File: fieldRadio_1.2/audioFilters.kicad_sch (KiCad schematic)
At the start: 42 parts, among them U2 OPA1678, U3 OPA1678, U4 OPA1678, U5 OPA1678

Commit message: Starting to update fieldRadio 1.2 schematics
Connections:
- net HPLP Filters/in: no longer U5.6 (-), U5.7
- new net: U5.6 (-), U5.7

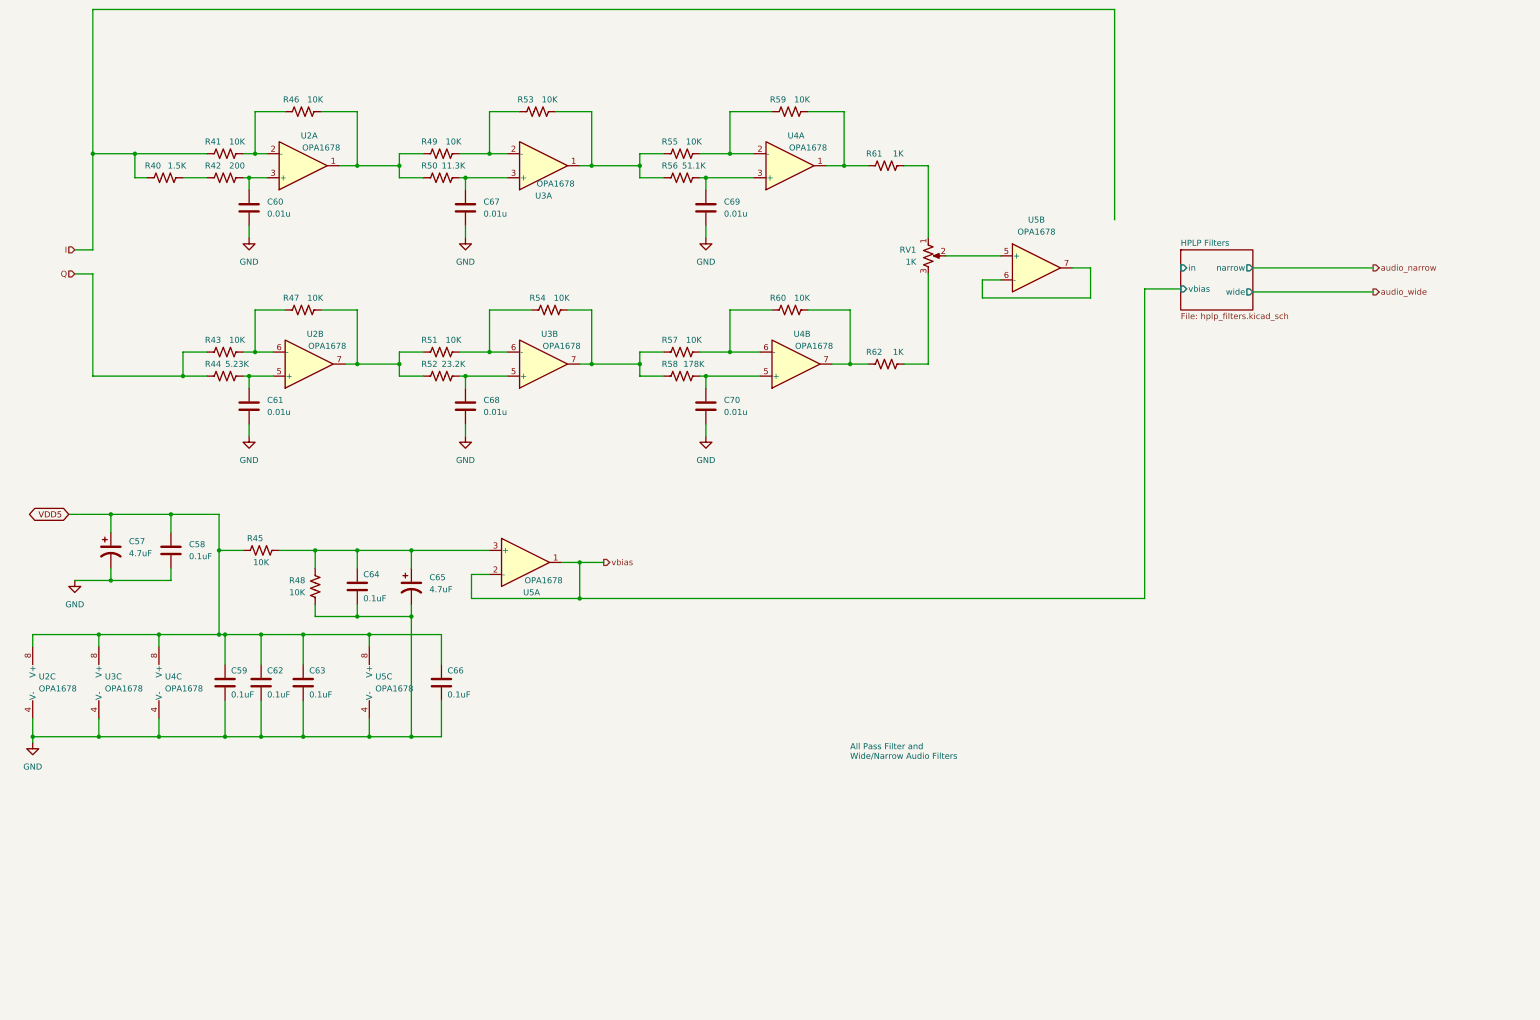
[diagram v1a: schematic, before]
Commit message: schematic audio work on the audio path
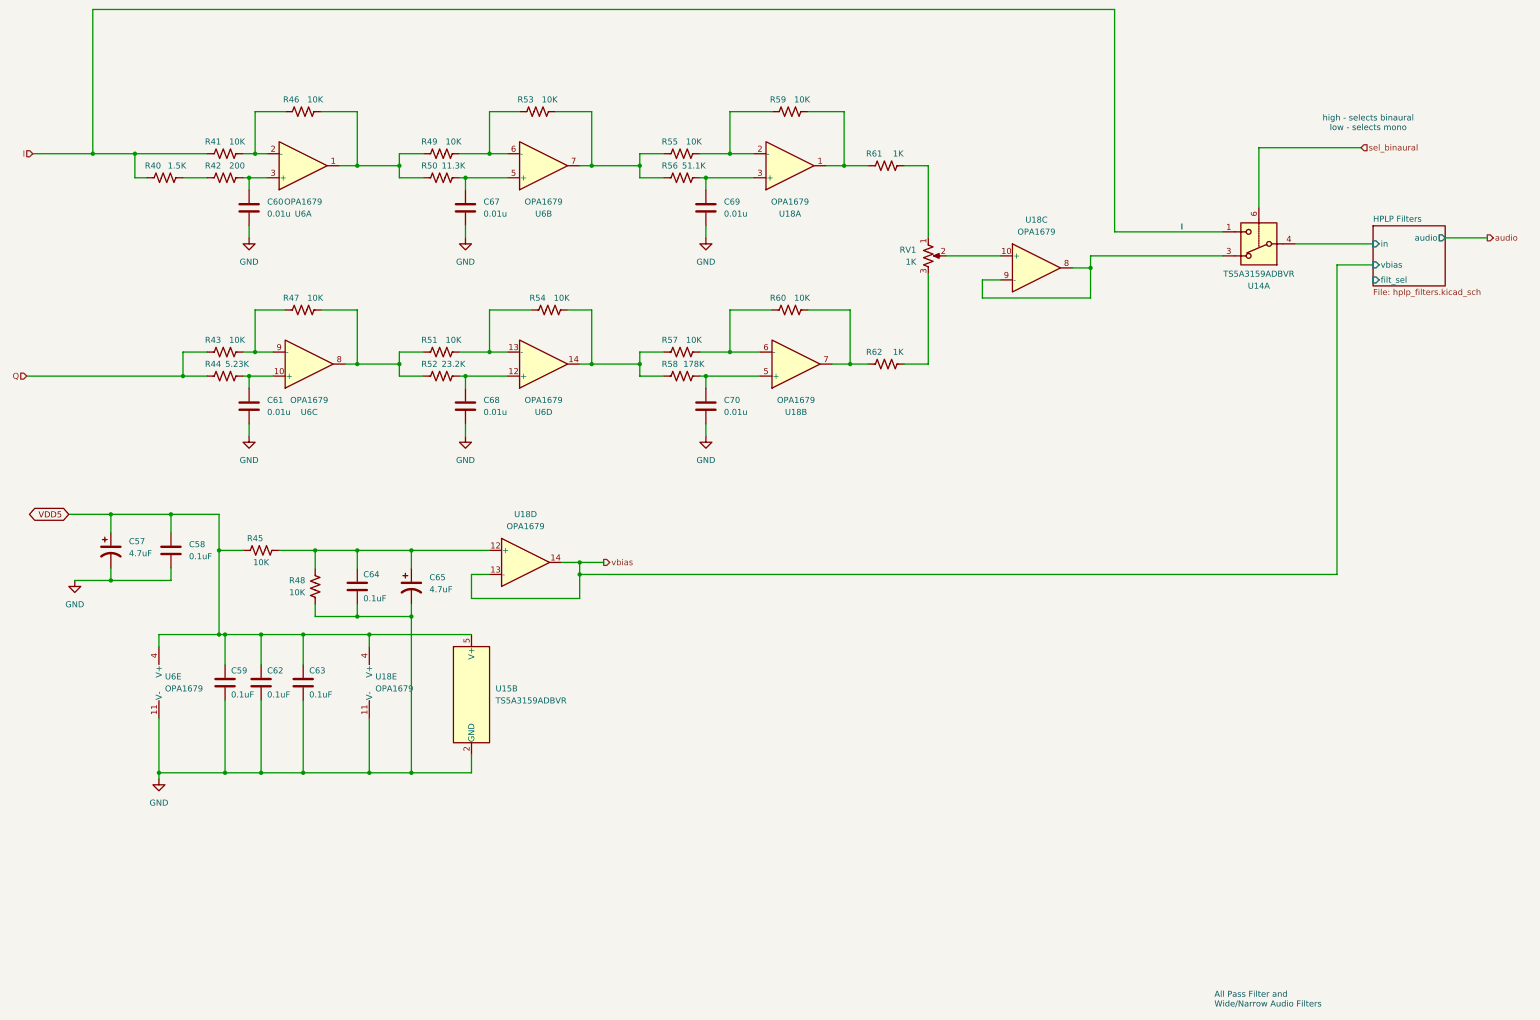
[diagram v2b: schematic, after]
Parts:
- removed C66: 0.1uF, Capacitor_SMD:C_0603_1608Metric_Pad1.08x0.95mm_HandSolder, symbol Device:C
- removed U2, U3, U4, U5: OPA1678, Package_SO:SOIC-8_3.9x4.9mm_P1.27mm, symbol Amplifier_Operational:OPA1678
- added U14, U15: TS5A3159ADBVR, Package_TO_SOT_SMD:SOT-23-6, symbol Analog_Switch:TS5A3159ADBVR
- added U18, U6: OPA1679, symbol Amplifier_Operational:OPA1679
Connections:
- net GND: now also U15.2 (GND), U18.11 (V-), U6.11 (V-)
- net HPLP Filters/in: now also U14.4
- net I: now also U14.1
- net VDD5: now also U15.5 (V+), U18.4 (V+), U6.4 (V+)
- net vbias: now also U18.13 (-), U18.14
- net at C68.1, R52.2: now also U6.12 (+)
- net at RV1.2: now also U18.10 (+)
- net at R59.2, R61.1: now also U18.1
- net at R49.2, R53.1: now also U6.6 (-)
- net at R53.2, R55.1, R56.1: now also U6.7
- net at C60.1, R42.2: now also U6.3 (+)
- net at C61.1, R44.2: now also U6.10 (+)
- net at R43.2, R47.1: now also U6.9 (-)
- net at R47.2, R51.1, R52.1: now also U6.8
- net at R55.2, R59.1: now also U18.2 (-)
- net at C69.1, R56.2: now also U18.3 (+)
- net at R51.2, R54.1: now also U6.13 (-)
- net at R41.2, R46.1: now also U6.2 (-)
- net at C67.1, R50.2: now also U6.5 (+)
- net at R46.2, R49.1, R50.1: now also U6.1
- net at R54.2, R57.1, R58.1: now also U6.14
- net at R57.2, R60.1: now also U18.6 (-)
- net at C70.1, R58.2: now also U18.5 (+)
- net at C64.1, C65.1, R45.2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: now also U18.12 (+)
- net at R60.2, R62.1: now also U18.7
- new net: U14.3, U18.8, U18.9 (-)
- new net sel_binaural: U14.6
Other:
- sheet HPLP Filters ports: added audio, filt_sel; removed narrow, wide
- note added: "high - selects binaural low - selects mono"
